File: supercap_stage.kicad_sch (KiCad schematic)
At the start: 10 parts, among them Q3002 SS8050, U3002 LMV321-TR

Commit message: Renumber all sheets
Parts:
- renumbered C3003 to C3001, C3004 to C3002, D3002 to D3001, Q3002 to Q3001, R3006 to R3001, R3007 to R3002, R3008 to R3003, R3009 to R3004, R3010 to R3005, U3002 to U3001
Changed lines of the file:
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@@
 		(dnp no)
 		(fields_autoplaced yes)
-		(property "Reference" "#FLG03002"
+		(property "Reference" "#FLG03001"
 			(at 152.4 78.105 0)
 			(effects
@@
 		(on_board yes)
 		(dnp no)
-		(property "Reference" "C3004"
+		(property "Reference" "C3002"
 			(at 192.2272 92.8116 0)
 			(effects
@@
 		(dnp no)
 		(fields_autoplaced yes)
-		(property "Reference" "R3006"
+		(property "Reference" "R3001"
 			(at 85.09 92.7099 0)
 			(effects
@@
 		(dnp no)
 		(fields_autoplaced yes)
-		(property "Reference" "C3003"
+		(property "Reference" "C3001"
 			(at 161.29 86.3599 0)
 			(effects
@@
 		(dnp no)
 		(fields_autoplaced yes)
-		(property "Reference" "R3009"
+		(property "Reference" "R3004"
 			(at 107.95 85.0899 0)
 			(effects
@@
 		(on_board yes)
 		(dnp no)
-		(property "Reference" "Q3002"
+		(property "Reference" "Q3001"
 			(at 134.3914 92.8116 0)
 			(effects
@@
 		(dnp no)
 		(fields_autoplaced yes)
-		(property "Reference" "R3010"
+		(property "Reference" "R3005"
 			(at 107.95 100.3299 0)
 			(effects
@@
 		(dnp no)
 		(fields_autoplaced yes)
-		(property "Reference" "R3007"
+		(property "Reference" "R3002"
 			(at 96.52 85.0899 0)
 			(effects
@@
 		(dnp no)
 		(fields_autoplaced yes)
-		(property "Reference" "R3008"
+		(property "Reference" "R3003"
 			(at 96.52 97.7899 0)
 			(effects
@@
 		(on_board yes)
 		(dnp no)
-		(property "Reference" "U3002"
+		(property "Reference" "U3001"
 			(at 120.65 86.36 0)
 			(effects
@@
 		(dnp no)
 		(fields_autoplaced yes)
-		(property "Reference" "D3002"
+		(property "Reference" "D3001"
 			(at 149.86 97.4724 90)
 			(effects

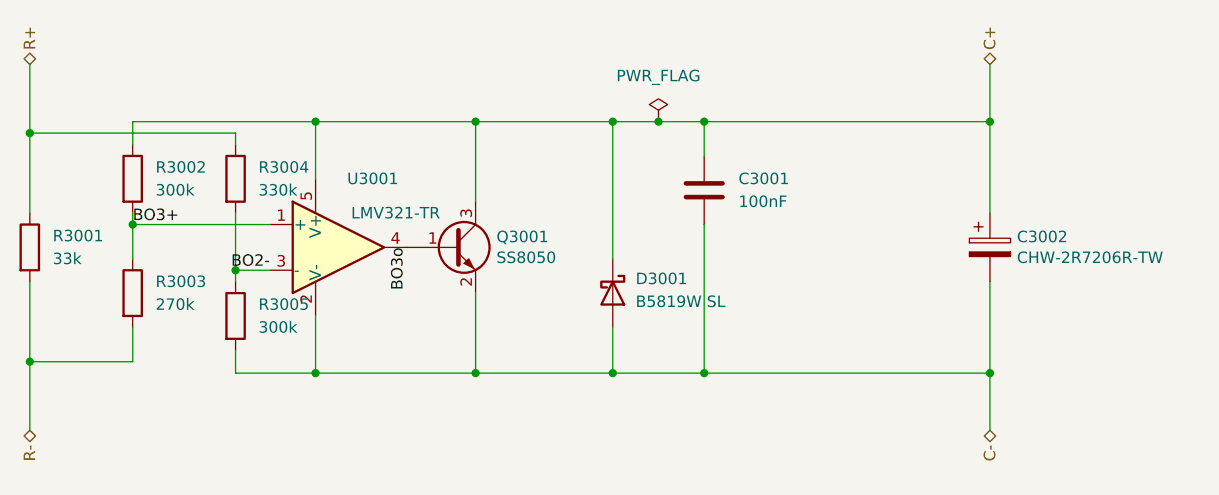
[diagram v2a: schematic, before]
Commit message: Reannotate components
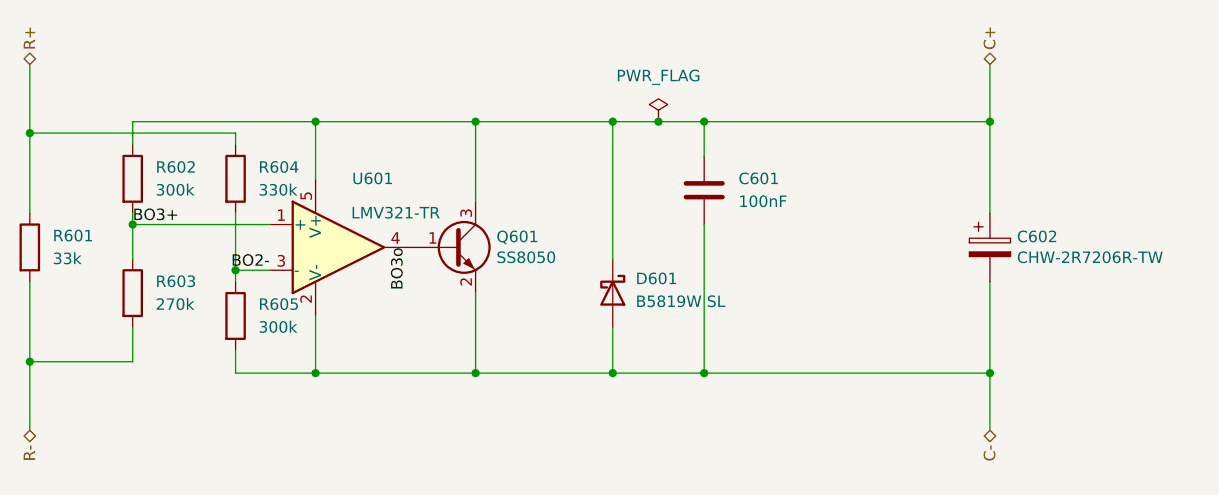
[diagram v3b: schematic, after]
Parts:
- renumbered C3001 to C601, C3002 to C602, D3001 to D601, Q3001 to Q601, R3001 to R601, R3002 to R602, R3003 to R603, R3004 to R604, R3005 to R605, U3001 to U601

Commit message: Silkscreen mostly done
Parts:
- C601: value 100nF -> 1uF; LCSC C1525 -> C52923
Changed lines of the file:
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@@
 			)
 		)
-		(property "Value" "100nF"
+		(property "Value" "1uF"
 			(at 161.29 88.8999 0)
 			(effects
@@
 			)
 		)
-		(property "LCSC" "C1525"
+		(property "LCSC" "C52923"
 			(at 157.48 87.63 0)
 			(effects

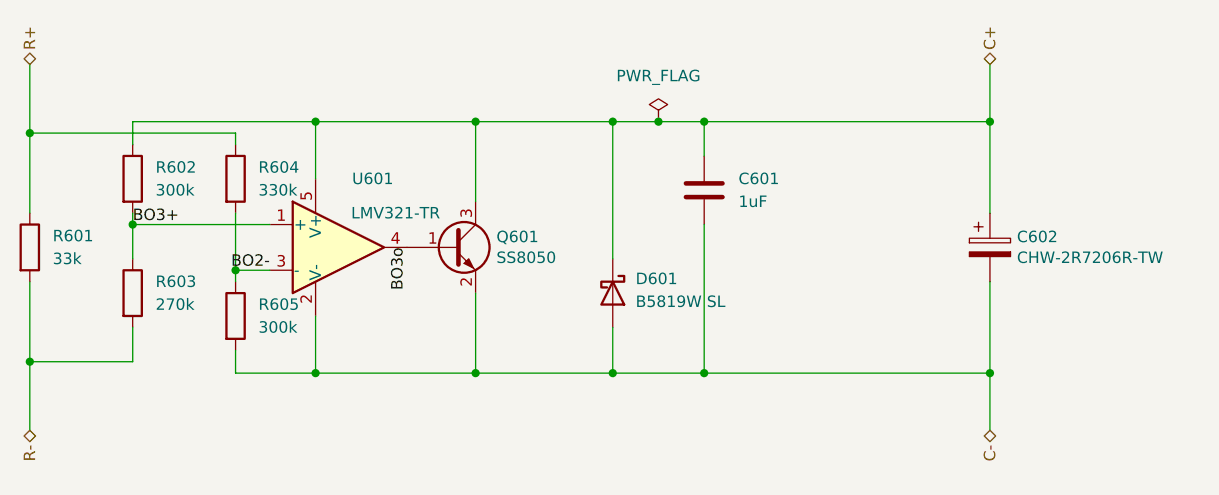
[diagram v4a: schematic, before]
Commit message: Finish the board redesign with SoM on the bottom
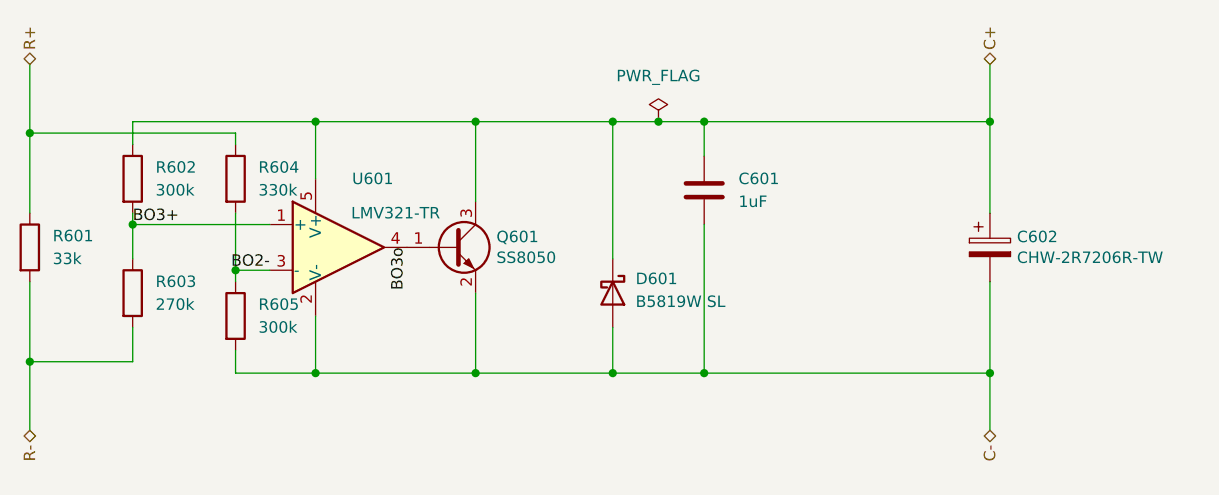
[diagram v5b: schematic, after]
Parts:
- D601: footprint Diode_SMD:D_SOD-123 -> Diode_SMD:D_SMA
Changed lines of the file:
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@@
 			)
 		)
-		(property "Description" ""
+		(property "Description" "Polarized capacitor"
 			(at 189.23 93.98 0)
 			(effects
@@
 			)
 		)
-		(property "Description" ""
+		(property "Description" "Resistor"
 			(at 82.55 93.98 0)
 			(effects
@@
 			)
 		)
-		(property "Description" ""
+		(property "Description" "Unpolarized capacitor"
 			(at 157.48 87.63 0)
 			(effects
@@
 			)
 		)
-		(property "Description" ""
+		(property "Description" "Resistor"
 			(at 105.41 86.36 0)
 			(effects
@@
 			)
 		)
-		(property "Datasheet" "https://www.lcsc.com/datasheet/lcsc_datasheet_2303221100_Jiangsu-Changjing-Electronics-Technology-Co---Ltd--SS8050-RANGE-200-350_C2150.pdf"
+		(property "Datasheet" "www.onsemi.com/pub/Collateral/MMBT5550LT1-D.PDF"
 			(at 129.54 93.98 0)
 			(effects
@@
 			)
 		)
-		(property "Description" ""
+		(property "Description" "0.6A Ic, 160V Vce, NPN Transistor, SOT-23"
 			(at 129.54 93.98 0)
 			(effects
@@
 			)
 		)
-		(property "Description" ""
+		(property "Description" "Resistor"
 			(at 105.41 101.6 0)
 			(effects
@@
 			)
 		)
-		(property "Description" ""
+		(property "Description" "Resistor"
 			(at 93.98 86.36 0)
 			(effects
@@
 			)
 		)
-		(property "Description" ""
+		(property "Description" "Low-Voltage Rail-to-Rail Output Operational Amplifiers, SOT-23-5/SC-70-5"
 			(at 116.84 93.98 0)
 			(effects
@@
 			)
 		)
-		(property "Footprint" "Diode_SMD:D_SOD-123"
+		(property "Footprint" "Diode_SMD:D_SMA"
 			(at 142.875 99.06 0)
 			(effects

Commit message: Further refinements
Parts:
- added TP3804: TestPoint, TestPoint:TestPoint_Pad_1.5x1.5mm, symbol Connector:TestPoint
- added TP3808: TestPoint, TestPoint:TestPoint_Pad_D1.5mm, symbol Connector:TestPoint
- added TP601: TestPoint, TestPoint:TestPoint_Pad_D1.0mm, symbol Connector:TestPoint
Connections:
- net BO3o: now also TP601.1
- net C+: now also TP3804.1
- net C-: now also TP3808.1
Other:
- moved on the sheet: Q601

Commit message: Finish transitioning to RP2040
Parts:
- D601: value B5819W SL -> B5819W; footprint Diode_SMD:D_SMA -> Diode_SMD:D_SOD-123
- renumbered TP3804 to TP602, TP3808 to TP603
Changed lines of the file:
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@@
 		(on_board yes)
 		(dnp no)
-		(property "Reference" "TP3808"
+		(property "Reference" "TP603"
 			(at 172.72 105.9181 0)
 			(effects
@@
 			(project "HALPI2"
 				(path "/abc482bd-3f17-4d35-80db-1da3dcdb5c27/c7bf4e1f-6bd1-4be7-9e56-1bd438bf5d42/07643414-c558-4752-92d9-19f7e64f0193/1e769c60-9395-4585-ba88-98ef14b595bd"
-					(reference "TP3811")
+					(reference "TP903")
 					(unit 1)
 				)
 				(path "/abc482bd-3f17-4d35-80db-1da3dcdb5c27/c7bf4e1f-6bd1-4be7-9e56-1bd438bf5d42/07643414-c558-4752-92d9-19f7e64f0193/3f9b067f-2b82-4260-ad8a-665c0f191623"
-					(reference "TP3809")
+					(reference "TP703")
 					(unit 1)
 				)
 				(path "/abc482bd-3f17-4d35-80db-1da3dcdb5c27/c7bf4e1f-6bd1-4be7-9e56-1bd438bf5d42/07643414-c558-4752-92d9-19f7e64f0193/814ce5bc-699b-4608-b12b-d1ea1de7e475"
-					(reference "TP3808")
+					(reference "TP603")
 					(unit 1)
 				)
 				(path "/abc482bd-3f17-4d35-80db-1da3dcdb5c27/c7bf4e1f-6bd1-4be7-9e56-1bd438bf5d42/07643414-c558-4752-92d9-19f7e64f0193/98212110-a878-47c3-ba60-a4b4dcdefdc6"
-					(reference "TP3810")
+					(reference "TP803")
 					(unit 1)
 				)
@@
 		(on_board yes)
 		(dnp no)
-		(property "Reference" "TP3804"
+		(property "Reference" "TP602"
 			(at 172.72 77.9781 0)
 			(effects
@@
 			(project "HALPI2"
 				(path "/abc482bd-3f17-4d35-80db-1da3dcdb5c27/c7bf4e1f-6bd1-4be7-9e56-1bd438bf5d42/07643414-c558-4752-92d9-19f7e64f0193/1e769c60-9395-4585-ba88-98ef14b595bd"
-					(reference "TP3807")
+					(reference "TP902")
 					(unit 1)
 				)
 				(path "/abc482bd-3f17-4d35-80db-1da3dcdb5c27/c7bf4e1f-6bd1-4be7-9e56-1bd438bf5d42/07643414-c558-4752-92d9-19f7e64f0193/3f9b067f-2b82-4260-ad8a-665c0f191623"
-					(reference "TP3805")
+					(reference "TP702")
 					(unit 1)
 				)
 				(path "/abc482bd-3f17-4d35-80db-1da3dcdb5c27/c7bf4e1f-6bd1-4be7-9e56-1bd438bf5d42/07643414-c558-4752-92d9-19f7e64f0193/814ce5bc-699b-4608-b12b-d1ea1de7e475"
-					(reference "TP3804")
+					(reference "TP602")
 					(unit 1)
 				)
 				(path "/abc482bd-3f17-4d35-80db-1da3dcdb5c27/c7bf4e1f-6bd1-4be7-9e56-1bd438bf5d42/07643414-c558-4752-92d9-19f7e64f0193/98212110-a878-47c3-ba60-a4b4dcdefdc6"
-					(reference "TP3806")
+					(reference "TP802")
 					(unit 1)
 				)
@@
 			)
 		)
-		(property "Value" "B5819W SL"
+		(property "Value" "B5819W"
 			(at 149.86 100.0124 90)
 			(effects
@@
 			)
 		)
-		(property "Footprint" "Diode_SMD:D_SMA"
+		(property "Footprint" "Diode_SMD:D_SOD-123"
 			(at 142.875 99.06 0)
 			(effects
